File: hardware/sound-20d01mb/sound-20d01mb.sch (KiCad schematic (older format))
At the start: 9 parts

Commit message: Updated PSU
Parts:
- added J?: Conn_01x02, Connector_JST:JST_XH_B02B-XH-A_1x02_P2.50mm_Vertical, symbol Connector_Generic:Conn_01x02
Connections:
- net GNDD: now also J?.2 (Pin_2)
- new net Power Supply Unit/EXT_5V: J?.1 (Pin_1)
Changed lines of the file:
@@
 F0 "Power Supply Unit" 50
 F1 "psu.sch" 50
+F2 "EXT_5V" I R 3650 4600 50
 $EndSheet
 $Comp
@@
 Wire Wire Line
 	1700 3450 2450 3450
+$Comp
+L Connector_Generic:Conn_01x02 J?
+U 1 1 60EA1B68
+P 4200 4600
+F 0 "J?" H 4280 4592 50  0000 L CNN
+F 1 "Conn_01x02" H 4280 4501 50  0000 L CNN
+F 2 "Connector_JST:JST_XH_B02B-XH-A_1x02_P2.50mm_Vertical" H 4200 4600 50  0001 C CNN
+F 3 "~" H 4200 4600 50  0001 C CNN
+	1    4200 4600
+	1    0    0    -1
+$EndComp
+$Comp
+L power:GNDD #PWR?
+U 1 1 60EA1BF4
+P 3900 4800
+F 0 "#PWR?" H 3900 4550 50  0001 C CNN
+F 1 "GNDD" H 3904 4645 50  0000 C CNN
+F 2 "" H 3900 4800 50  0001 C CNN
+F 3 "" H 3900 4800 50  0001 C CNN
+	1    3900 4800
+	1    0    0    -1
+$EndComp
+Wire Wire Line
+	4000 4700 3900 4700
+Wire Wire Line
+	3900 4700 3900 4800
+Wire Wire Line
+	4000 4600 3650 4600
 $EndSCHEMATC

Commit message: Updated text
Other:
- note added: "External 5V Power supply (digital)"
- note added: "Supply voltage range: 12V to 30V (analog)"
- note removed: "Supply voltage range: 12V to 30V"
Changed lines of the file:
@@
 	6450 3400 6450 3300
 Text Notes 6700 3300 0    50   ~ 0
-Supply voltage range: 12V to 30V
+Supply voltage range: 12V to 30V (analog)
 $Comp
 L power:VBUS #PWR?
@@
 Wire Wire Line
 	4000 4600 3650 4600
+Text Notes 4150 4500 0    50   ~ 0
+External 5V Power supply (digital)
 $EndSCHEMATC

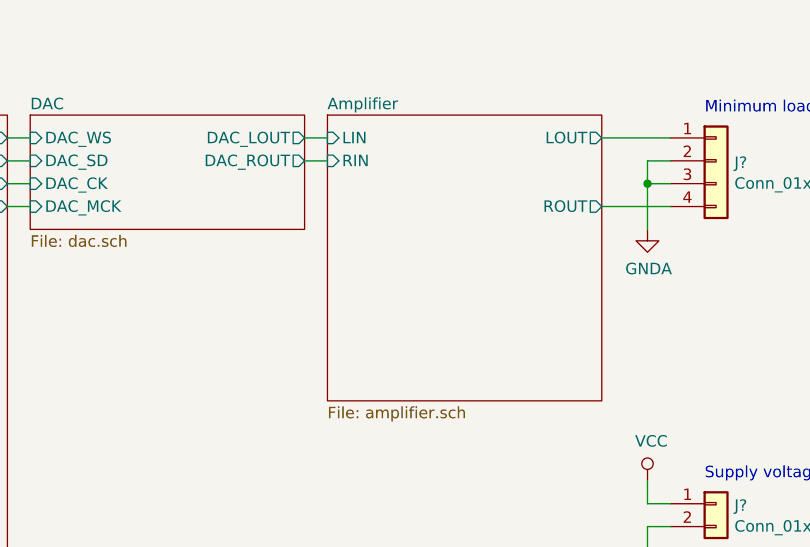
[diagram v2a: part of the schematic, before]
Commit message: Added PC817
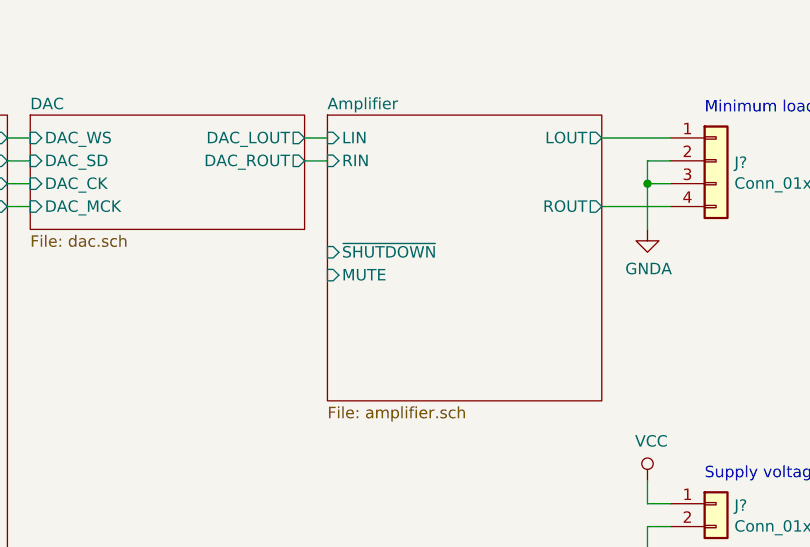
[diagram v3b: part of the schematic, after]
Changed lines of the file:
@@
 F4 "LOUT" O R 6250 1800 50
 F5 "ROUT" O R 6250 2100 50
+F6 "~SHUTDOWN" I L 5050 2300 50
+F7 "MUTE" I L 5050 2400 50
 $EndSheet
 $Comp

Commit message: Added OSC
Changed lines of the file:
@@
 $EndSheet
 $Sheet
-S 5050 1700 1200 1250
+S 5050 1700 1200 500
 U 60DE2DF4
 F0 "Amplifier" 50
@@
 F4 "LOUT" O R 6250 1800 50
 F5 "ROUT" O R 6250 2100 50
-F6 "~SHUTDOWN" I L 5050 2300 50
-F7 "MUTE" I L 5050 2400 50
 $EndSheet
 $Comp

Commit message: Added X977B04
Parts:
- J?: footprint (none) -> sound-20d01mb:X977B04
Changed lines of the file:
@@
 F 0 "J?" H 6830 1892 50  0000 L CNN
 F 1 "Conn_01x04" H 6830 1801 50  0000 L CNN
-F 2 "" H 6750 1900 50  0001 C CNN
+F 2 "sound-20d01mb:X977B04" H 6750 1900 50  0001 C CNN
 F 3 "~" H 6750 1900 50  0001 C CNN
 	1    6750 1900

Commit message: Updated schematic
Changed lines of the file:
@@
 F11 "SAI1_MCLK_B" O R 3650 2100 50
 F12 "SWO" O L 2450 3450 50
+F13 "PA4_NSS" B R 3650 2600 50
+F14 "PA5_SCK" B R 3650 2700 50
+F15 "PA6_MISO" B R 3650 2800 50
+F16 "PA7_MOSI" B R 3650 2900 50
+F17 "PB0_SDIO_D1" B R 3650 3350 50
+F18 "PB1_SDIO_D2" B R 3650 3450 50
+F19 "PB2_SDIO_CK" B R 3650 3150 50
+F20 "PC8_SDIO_D0" B R 3650 3250 50
+F21 "PD2_SDIO_CMD" B R 3650 3050 50
+F22 "PC11_SDIO_D3" B R 3650 3550 50
+F23 "~SHUTDOWN" O R 3650 2350 50
+F24 "MUTE" O R 3650 2450 50
 $EndSheet
 $Sheet
@@
 $EndSheet
 $Sheet
-S 5050 1700 1200 500
+S 5050 1700 1200 850
 U 60DE2DF4
 F0 "Amplifier" 50
@@
 F4 "LOUT" O R 6250 1800 50
 F5 "ROUT" O R 6250 2100 50
+F6 "~SHUTDOWN" I L 5050 2350 50
+F7 "MUTE" I L 5050 2450 50
 $EndSheet
 $Comp
@@
 Text Notes 4150 4500 0    50   ~ 0
 External 5V Power supply (digital)
+Wire Wire Line
+	3650 2350 5050 2350
+Wire Wire Line
+	3650 2450 5050 2450
 $EndSCHEMATC

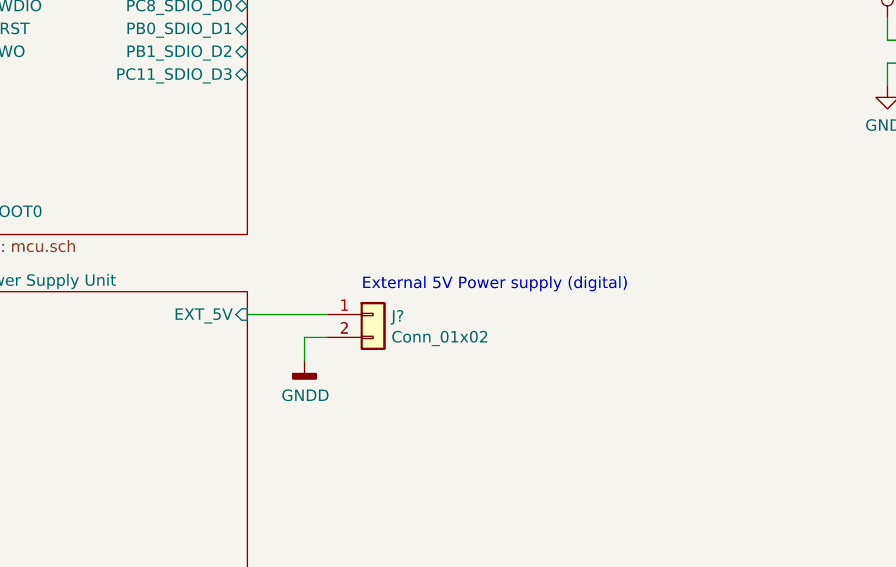
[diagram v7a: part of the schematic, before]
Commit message: Added fuse for USB
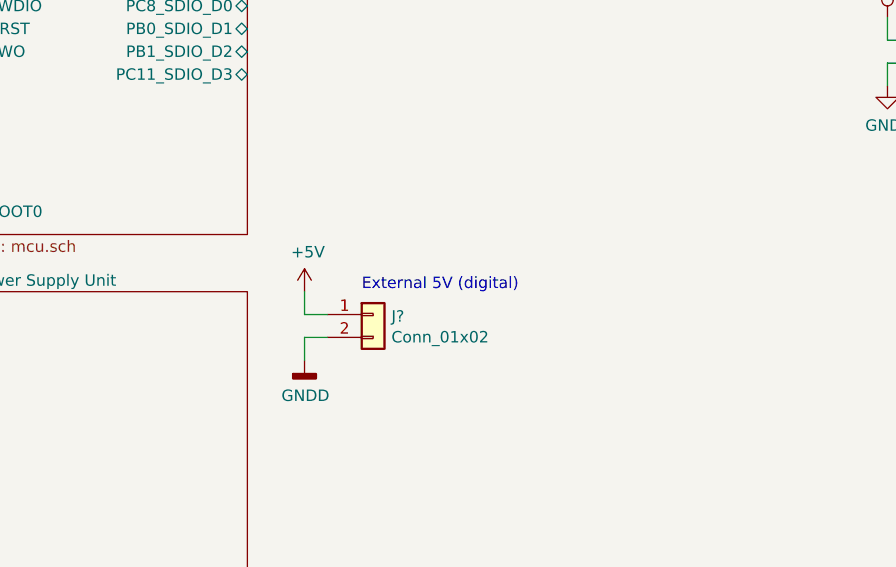
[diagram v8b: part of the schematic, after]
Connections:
- net Power Supply Unit/EXT_5V renamed +5V
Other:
- note added: "External 5V (digital)"
- note removed: "External 5V Power supply (digital)"
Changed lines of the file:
@@
 F0 "Power Supply Unit" 50
 F1 "psu.sch" 50
-F2 "EXT_5V" I R 3650 4600 50
 $EndSheet
 $Comp
@@
 	1    0    0    -1
 $EndComp
-Wire Wire Line
-	1950 1600 2050 1600
-Wire Wire Line
-	2050 1600 2050 1500
 Wire Wire Line
 	1950 1800 2450 1800
@@
 Wire Wire Line
 	3900 4700 3900 4800
-Wire Wire Line
-	4000 4600 3650 4600
 Text Notes 4150 4500 0    50   ~ 0
-External 5V Power supply (digital)
+External 5V (digital)
 Wire Wire Line
 	3650 2350 5050 2350
 Wire Wire Line
 	3650 2450 5050 2450
+$Comp
+L power:+5V #PWR?
+U 1 1 6153EEDC
+P 3900 4500
+F 0 "#PWR?" H 3900 4350 50  0001 C CNN
+F 1 "+5V" H 3915 4673 50  0000 C CNN
+F 2 "" H 3900 4500 50  0001 C CNN
+F 3 "" H 3900 4500 50  0001 C CNN
+	1    3900 4500
+	1    0    0    -1
+$EndComp
+Wire Wire Line
+	4000 4600 3900 4600
+Wire Wire Line
+	3900 4600 3900 4500
+Wire Wire Line
+	1950 1600 2050 1600
+Wire Wire Line
+	2050 1600 2050 1500
 $EndSCHEMATC
